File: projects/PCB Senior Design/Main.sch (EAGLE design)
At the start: 70 parts, among them J8 U.FL, J9 NANO_SIM, Q2 8MHz, Q3 2.5A/30V/105mΩ, U1 UBLOX_SAM_M8Q-0-10, U2 32KB NRF51822, U4 TCA9406DCU, U5 MCP73831, U6 SARA-R410M-2B, U7 TXB0104, U9 AP7361C-33FGE, Y1 32.768kHz (535-9166-2-ND)

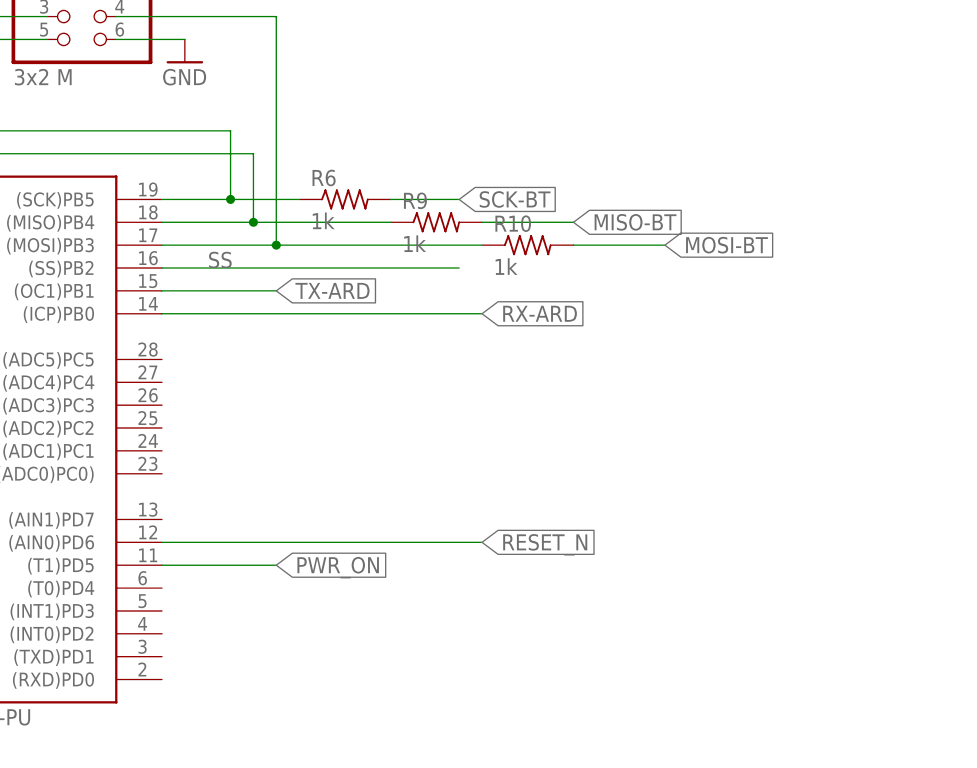
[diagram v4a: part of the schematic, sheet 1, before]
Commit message: Changes to BT connection
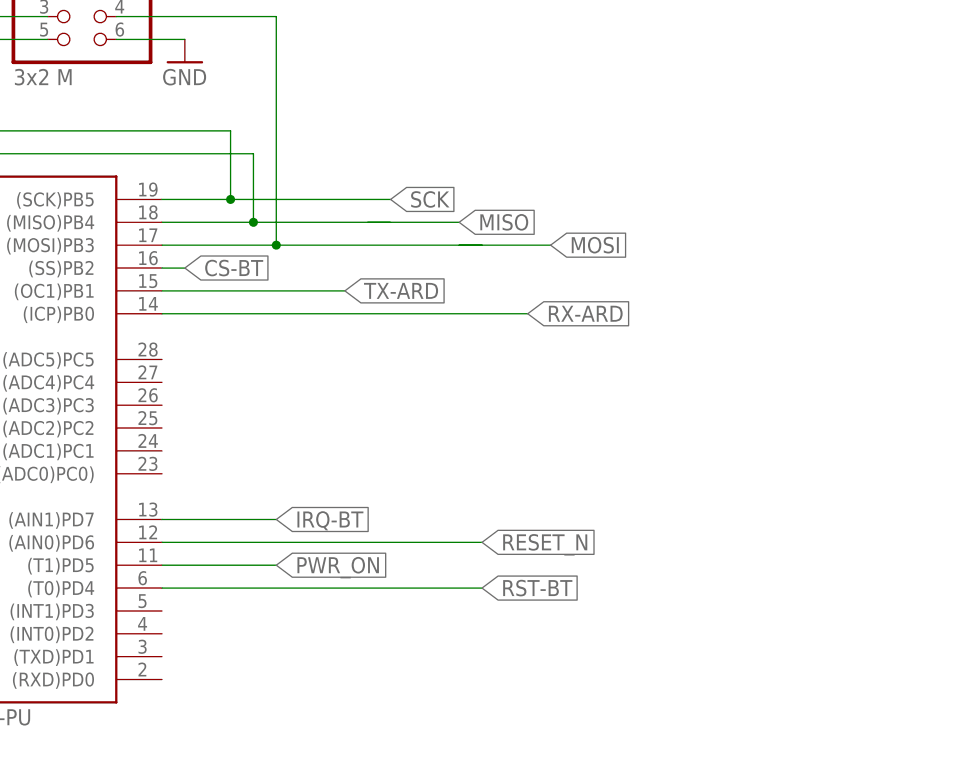
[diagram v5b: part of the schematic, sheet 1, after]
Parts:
- removed D11: 1N4148, microbuilder:DIODESOD-323
- removed R10, R6, R9: 1k, rcl:R-US_R0201
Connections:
- removed net CS_5V: D11.C
- removed net DFU_3V: U2.P0.07
- removed net MISO-BT: R9.2, U2.P0.22
- removed net MOSI-BT: R10.2, U2.P0.23
- removed net SCK-BT: R6.2, U2.P0.21
- removed net SS: ZU4.(SS)PB2
- removed net SWDIO/RST_3V: U2.SWDIO/NRESET
- new net RST-BT: U2.SWDIO/NRESET, ZU4.(T0)PD4
- net CS-BT: now also ZU4.(SS)PB2; no longer D11.A
- net IRQ-BT: now also ZU4.(AIN1)PD7
- net MISO: now also U2.P0.22; no longer R9.1
- net MOSI: now also U2.P0.23; no longer R10.1
- net SCK: now also U2.P0.21; no longer R6.1

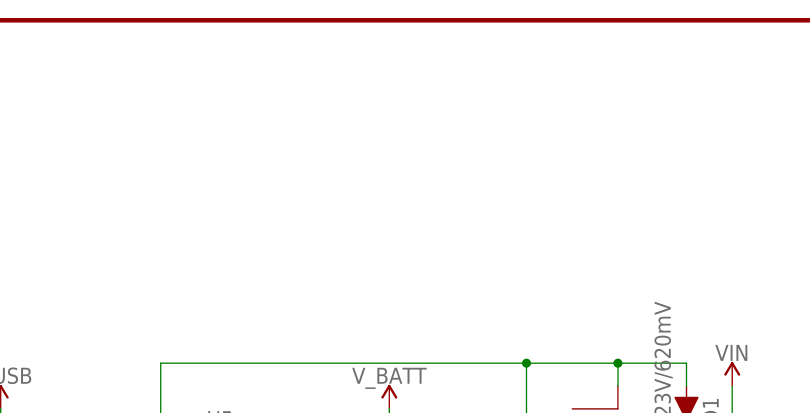
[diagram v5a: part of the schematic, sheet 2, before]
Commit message: Added DPDT and potentiometer
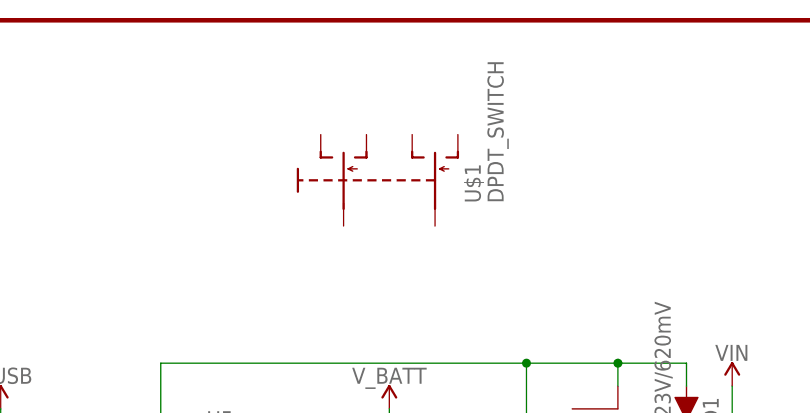
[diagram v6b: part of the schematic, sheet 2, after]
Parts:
- added U$1: DPDT_SWITCH, SeniorDesign:DPDT_SWITCH
- added U$3: 10k, SeniorDesign:POTENTIOMETER
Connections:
- new net PING-POT: U$3.P$3, ZU4.(ADC0)PC0)
- net 3.3V: now also U$3.P$1
- net GND: now also U$3.P$2
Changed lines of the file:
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@@
 <?xml version="1.0" encoding="utf-8"?>
 <!DOCTYPE eagle SYSTEM "eagle.dtd">
-<eagle version="9.6.0">
+<eagle version="9.6.2">
 <drawing>
 <settings>
@@
 <part name="GND37" library="SparkFun-PowerSymbols" deviceset="GND" device=""/>
 <part name="L2" library="ublox" deviceset="INDUCTOR" device="-0603-68NH" value="DNP"/>
-<part name="FRAME2" library="SparkFun-Aesthetics" deviceset="FRAME-LETTER" device=""/>
+<part name="FRAME2" library="SparkFun-Aesthetics" library_urn="urn:adsk.eagle:library:507" deviceset="FRAME-LETTER" device="" package3d_urn="urn:adsk.eagle:package:41384561/3"/>
 <part name="C8" library="SparkFun-Capacitors" deviceset="0.1UF" device="-0603-25V-(+80/-20%)" value="0.1uF"/>
 <part name="C9" library="SparkFun-Capacitors" deviceset="10NF" device="-0603-50V-10%" value="10nF"/>
@@
 <part name="C30" library="SmartPrj" deviceset="C-EU" device="0603-RND" value="22p"/>
 <part name="GND32" library="supply1" deviceset="GND" device=""/>
+<part name="SUPPLY11" library="SparkFun-PowerSymbols" library_urn="urn:adsk.eagle:library:530" deviceset="3.3V" device=""/>
+<part name="GND5" library="supply1" deviceset="GND" device=""/>
+<part name="U$3" library="SeniorDesign" deviceset="POTENTIOMETER" device="" value="10k"/>
+<part name="U$1" library="SeniorDesign" deviceset="DPDT_SWITCH" device=""/>
 </parts>
 <sheets>
@@
 <attribute name="VALUE" x="-58.42" y="20.32" size="1.778" layer="96" rot="R270"/>
 </instance>
+<instance part="SUPPLY11" gate="G$1" x="93.98" y="2.54" smashed="yes">
+<attribute name="VALUE" x="93.98" y="5.334" size="1.778" layer="96" font="vector" align="bottom-center"/>
+</instance>
+<instance part="GND5" gate="1" x="93.98" y="-15.24" smashed="yes">
+<attribute name="VALUE" x="91.44" y="-17.78" size="1.778" layer="96"/>
+</instance>
+<instance part="U$3" gate="G$1" x="93.98" y="-5.08" smashed="yes" rot="R270">
+<attribute name="VALUE" x="88.9" y="-5.08" size="1.778" layer="96" rot="R270"/>
+<attribute name="NAME" x="99.06" y="2.54" size="1.778" layer="95" rot="R270"/>
+</instance>
 </instances>
 <busses>
@@
 <junction x="-53.34" y="17.78"/>
 </segment>
+<segment>
+<pinref part="GND5" gate="1" pin="GND"/>
+<pinref part="U$3" gate="G$1" pin="P$2"/>
+</segment>
 </net>
 <net name="SCK" class="0">
@@
 <wire x1="-33.02" y1="5.08" x2="-30.48" y2="5.08" width="0.1524" layer="91"/>
 <junction x="-30.48" y="5.08"/>
+</segment>
+<segment>
+<pinref part="SUPPLY11" gate="G$1" pin="3.3V"/>
+<pinref part="U$3" gate="G$1" pin="P$1"/>
 </segment>
 </net>
@@
 </segment>
 </net>
+<net name="PING-POT" class="0">
+<segment>
+<pinref part="ZU4" gate="G$1" pin="(ADC0)PC0)"/>
+<wire x1="17.78" y1="-5.08" x2="30.48" y2="-5.08" width="0.1524" layer="91"/>
+<label x="20.32" y="-5.08" size="1.778" layer="95"/>
+</segment>
+<segment>
+<wire x1="88.265" y1="-3.175" x2="76.2" y2="-3.175" width="0.1524" layer="91"/>
+<label x="76.2" y="-2.54" size="1.778" layer="95"/>
+<pinref part="U$3" gate="G$1" pin="P$3"/>
+</segment>
+</net>
 </nets>
 </sheet>
@@
 <attribute name="VALUE" x="68.58" y="5.334" size="1.778" layer="96" align="bottom-center"/>
 </instance>
+<instance part="U$1" gate="G$1" x="-15.24" y="30.48" smashed="yes">
+<attribute name="NAME" x="0" y="27.94" size="1.778" layer="95" rot="R90"/>
+<attribute name="VALUE" x="2.54" y="27.94" size="1.778" layer="96" rot="R90"/>
+</instance>
 </instances>

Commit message: Final touches
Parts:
- removed C16: DNP, SparkFun-Capacitors:27PF-0603-50V-5%
- removed J8: U.FL, SparkFun-Connectors:U.FL
- removed JP7: J-CHIP, SparkFun-Jumpers:JUMPER-SMT_2_NC_TRACE_NO-SILK
- removed JP8: J-U.FL, SparkFun-Jumpers:JUMPER-SMT_2_NO_NO-SILK
- removed L2: DNP, ublox:INDUCTOR-0603-68NH
- removed R8: DNP, SparkFun-Resistors:10KOHM-0603-1/10W-1%
- added R6: 10k, SparkFun-Resistors:10KOHM-0603-1/10W-1%
- added U$2: RGBLED_THRU, SeniorDesign:RGBLED_THRU
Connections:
- net PWR_ON renamed PWR-CELL
- net RESET_N renamed RST-CELL
- removed net N$2: R8.1, U6.ANT_DET
- removed net N$22: E1.SIGNAL, JP7.2
- removed net N$7: C16.1, L2.2, R8.2
- removed net N$9: J8.SIGNAL, JP8.2
- new net N$12: R6.2, U$1.O, U$1.S, U9.EN
- new net N$3: U$2.P$1, ZU4.(INT0)PD2
- new net N$4: U$2.P$3, ZU4.(TXD)PD1
- new net N$5: U$2.P$4, ZU4.(RXD)PD0
- net GND: now also R6.1, U$2.P$2; no longer C16.2, J8.GND@0, J8.GND@1
- net N$21: now also E1.SIGNAL; no longer JP7.1, JP8.1, L2.1
- net VIN: now also U$1.P; no longer U9.EN
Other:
- note added: "Assuming they can take 3.3V."
- note added: "Refer to datasheet for keepout area."
- note removed: "If ANT-DET is used: R8 = 10k C16 = 27pF L1 = 68nH C19 = 33pF"
- note removed: "JP7 and JP8 select either the on-board chip antenna, or an external antenna via the U.FL connector. (Only close ONE of these jumpers!) Default: JP8 (chip antenna)"
- note removed: "Must be enabled with: AT+UGPIOC=16,2"
- moved on the sheet: C26, C27, C7, D1, D12, D9, J1, J2, Q3, R1, R11, R15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

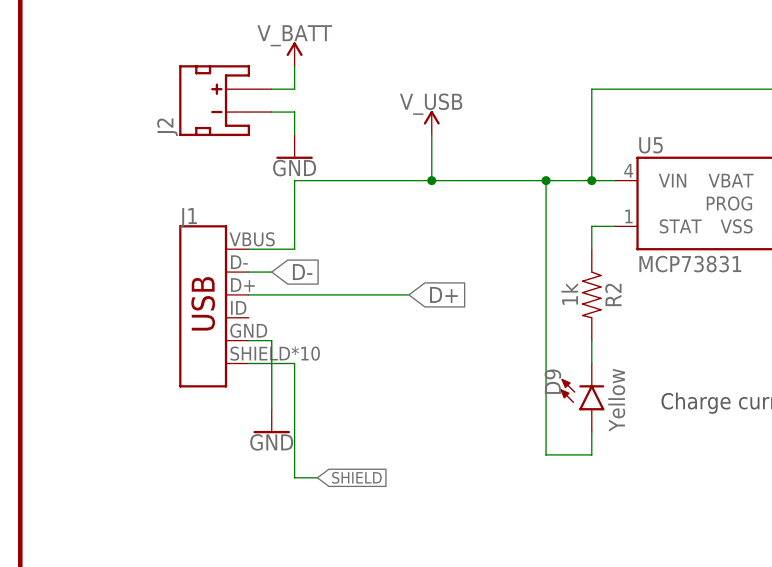
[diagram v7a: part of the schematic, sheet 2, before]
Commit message: removed usb data line
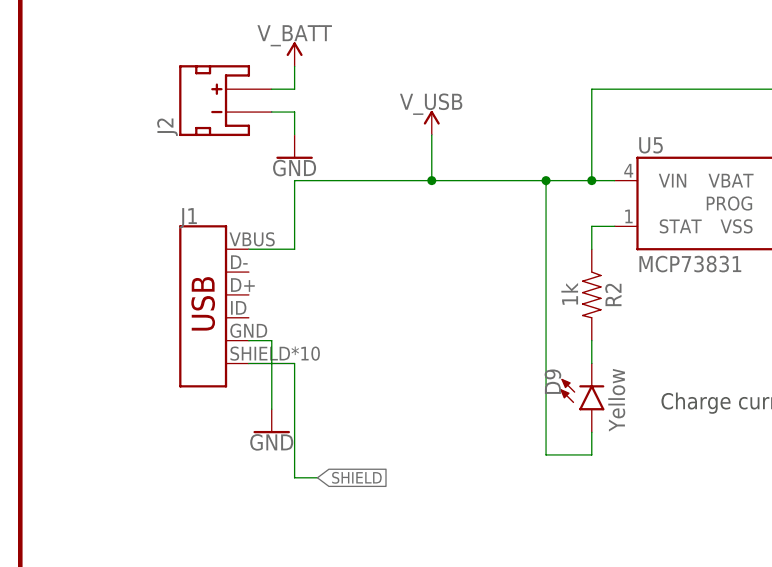
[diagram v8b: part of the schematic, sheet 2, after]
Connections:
- removed net D+: J1.D+
- removed net D-: J1.D-
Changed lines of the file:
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@@
-</segment>
-</net>
-<net name="D-" class="0">
-<segment>
-<pinref part="J1" gate="J1" pin="D-"/>
-<wire x1="-81.28" y1="-10.16" x2="-78.74" y2="-10.16" width="0.1524" layer="91"/>
-<label x="-78.74" y="-10.16" size="1.778" layer="95" xref="yes"/>
-</segment>
-</net>
-<net name="D+" class="0">
-<segment>
-<pinref part="J1" gate="J1" pin="D+"/>
-<label x="-63.5" y="-12.7" size="1.778" layer="95" xref="yes"/>
-<wire x1="-81.28" y1="-12.7" x2="-63.5" y2="-12.7" width="0.1524" layer="91"/>
 </segment>
 </net>
